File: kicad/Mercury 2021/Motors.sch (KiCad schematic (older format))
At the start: 13 parts, among them J15 Raspberry_Pi_2_3, J22 Servos_Connector, J23 Pi_Extra_Comm, J24 Pi_Extra_GPIO, J25 Pi_Extra_GPIO, J26 Pi_Extra_Power, J27 Pi_Extra_GND, J28 Pi_Extra_GPIO, J29 Pi_Extra_GPIO, J38 USB_B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

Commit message: Updated new board
- Did PCB traces
-- almost got away with just 2 copper layers, pi ruined it when there was only a bit to go. Probably possible but would take a lot of back and forth
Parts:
- added U12D1, U12E1: PCA9685, Connector_PinSocket_2.54mm:PinSocket_1x03_P2.54mm_Vertical, symbol Mercury:PCA9685
- J22: footprint Connector_PinSocket_2.54mm:PinSocket_2x03_P2.54mm_Vertical -> Connector_PinHeader_2.54mm:PinHeader_2x03_P2.54mm_Vertical; symbol Connector_Generic:Conn_02x03_Counter_Clockwise -> Connector_Generic:Conn_02x03_Top_Bottom
- U11, U13: footprint Connector_PinHeader_2.54mm:PinHeader_1x05_P2.54mm_Vertical -> Connector_JST:JST_EH_B5B-EH-A_1x05_P2.50mm_Vertical
- U12: footprint Connector_PinHeader_2.54mm:PinHeader_1x06_P2.54mm_Vertical -> Connector_PinSocket_2.54mm:PinSocket_1x06_P2.54mm_Vertical
- U12A1, U12B1: renamed from U12; footprint Connector_PinHeader_2.54mm:PinHeader_1x06_P2.54mm_Vertical -> Connector_PinSocket_2.54mm:PinSocket_1x03_P2.54mm_Vertical
- U12C1: renamed from U12; footprint Connector_PinHeader_2.54mm:PinHeader_1x06_P2.54mm_Vertical -> TerminalBlock:TerminalBlock_Altech_AK300-2_P5.00mm
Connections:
- net Serco_VCC is gone; now on net Servo_VCC: U12.5 (VCC)
- net Pi_5v: no longer J15.4 (5V), J26.1 (Pin_1), J26.2 (Pin_2)
- net Pi_GND: now also J15.39 (GND); no longer J15.20 (GND), J15.25 (GND), J15.30 (GND), J15.34 (GND), J27.1 (Pin_1), J27.2 (Pin_2), J27.3 (Pin_3), J27.4 (Pin_4), J27.5 (Pin_5)
- net at U12B1.1 (PWM_1): now also J22.4 (Pin_4); no longer J22.6 (Pin_6)
- net at U12B1.3 (GND): now also J22.6 (Pin_6); no longer J22.4 (Pin_4)
- net Pi_3v3 renamed Pi_3v3a
- net Pi_3v3a: no longer J15.17 (3V3), J26.5 (Pin_5)
- net SUB_D- renamed USB_D-
- new net Pi_3v3b: J15.17 (3V3), J26.5 (Pin_5)
- new net Pi_5v_a: J15.4 (5V), J26.2 (Pin_2)
- new net Pi_GNDa: J15.20 (GND), J27.5 (Pin_5)
- new net Pi_GNDb: J15.25 (GND), J27.4 (Pin_4)
- new net Pi_GNDc: J15.30 (GND), J27.3 (Pin_3)
- new net Pi_GNDe: J15.34 (GND), J27.2 (Pin_2)
- no-connect marks 4 -> 10
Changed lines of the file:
@@
 F 0 "U11" H 812 1075 50  0000 C CNN
 F 1 "PCA9685" H 812 984 50  0000 C CNN
-F 2 "Connector_PinHeader_2.54mm:PinHeader_1x05_P2.54mm_Vertical" H 750 1000 50  0001 C CNN
+F 2 "Connector_JST:JST_EH_B5B-EH-A_1x05_P2.50mm_Vertical" H 750 1000 50  0001 C CNN
 F 3 "" H 750 1000 50  0001 C CNN
 	3    750  800
@@
 F 0 "U13" H 812 2025 50  0000 C CNN
 F 1 "PCA9685" H 812 1934 50  0000 C CNN
-F 2 "Connector_PinHeader_2.54mm:PinHeader_1x05_P2.54mm_Vertical" H 750 1950 50  0001 C CNN
+F 2 "Connector_JST:JST_EH_B5B-EH-A_1x05_P2.50mm_Vertical" H 750 1950 50  0001 C CNN
 F 3 "" H 750 1950 50  0001 C CNN
 	3    750  1750
@@
 F 0 "U11" H 3119 1451 50  0000 L CNN
 F 1 "PCA9685" H 3119 1360 50  0000 L CNN
-F 2 "Connector_PinHeader_2.54mm:PinHeader_1x05_P2.54mm_Vertical" H 2800 1750 50  0001 C CNN
+F 2 "Connector_JST:JST_EH_B5B-EH-A_1x05_P2.50mm_Vertical" H 2800 1750 50  0001 C CNN
 F 3 "" H 2800 1750 50  0001 C CNN
 	1    2800 1550
@@
 F 0 "U13" H 3119 2051 50  0000 L CNN
 F 1 "PCA9685" H 3119 1960 50  0000 L CNN
-F 2 "Connector_PinHeader_2.54mm:PinHeader_1x05_P2.54mm_Vertical" H 2800 2350 50  0001 C CNN
+F 2 "Connector_JST:JST_EH_B5B-EH-A_1x05_P2.50mm_Vertical" H 2800 2350 50  0001 C CNN
 F 3 "" H 2800 2350 50  0001 C CNN
 	1    2800 2150
@@
 	5650 2200 5450 2200
 Entry Wire Line
-	5300 1700 5400 1800
+	5350 1700 5450 1800
 Entry Wire Line
 	5350 1900 5450 2000
@@
 Wire Bus Line
 	5350 2800 5350 3700
-$Comp
-L Mercury:PCA9685 U12
-U 2 1 609948C9
-P 3800 1300
-F 0 "U12" H 3969 950 50  0000 L CNN
-F 1 "PCA9685" H 3969 859 50  0000 L CNN
-F 2 "Connector_PinHeader_2.54mm:PinHeader_1x06_P2.54mm_Vertical" H 3800 1500 50  0001 C CNN
-F 3 "" H 3800 1500 50  0001 C CNN
-	2    3800 1300
-	-1   0    0    1
-$EndComp
 Entry Wire Line
 	3450 650  3350 750
@@
 AR Path="/6098200C" Ref="U?"  Part="3"
 AR Path="/609567C6/6098200C" Ref="U?"  Part="3"
-AR Path="/60979A3C/6098200C" Ref="U12"  Part="3"
-F 0 "U12" V 1000 1150 50  0000 L CNN
+AR Path="/60979A3C/6098200C" Ref="U12C1"  Part="3"
+F 0 "U12C1" V 1000 1150 50  0000 L CNN
 F 1 "PCA9685" V 900 1100 50  0000 L CNN
-F 2 "Connector_PinHeader_2.54mm:PinHeader_1x06_P2.54mm_Vertical" H 750 1450 50  0001 C CNN
+F 2 "TerminalBlock:TerminalBlock_Altech_AK300-2_P5.00mm" H 750 1450 50  0001 C CNN
 F 3 "" H 750 1450 50  0001 C CNN
 	3    750  1250
@@
 MotorPower
 $Comp
-L Connector_Generic:Conn_02x03_Counter_Clockwise J22
+L Connector_Generic:Conn_02x03_Top_Bottom J22
 U 1 1 609CB3BE
 P 4650 800
 F 0 "J22" H 4700 1117 50  0000 C CNN
 F 1 "Servos_Connector" H 4700 1026 50  0000 C CNN
-F 2 "Connector_PinSocket_2.54mm:PinSocket_2x03_P2.54mm_Vertical" H 4650 800 50  0001 C CNN
+F 2 "Connector_PinHeader_2.54mm:PinHeader_2x03_P2.54mm_Vertical" H 4650 800 50  0001 C CNN
 F 3 "~" H 4650 800 50  0001 C CNN
 	1    4650 800
 	1    0    0    -1
-$EndComp
-$Comp
-L Mercury:PCA9685 U12
-U 4 1 609BDBFC
-P 4550 800
-F 0 "U12" H 4708 484 50  0000 L CNN
-F 1 "PCA9685" H 4708 393 50  0000 L CNN
-F 2 "Connector_PinHeader_2.54mm:PinHeader_1x06_P2.54mm_Vertical" H 4550 1000 50  0001 C CNN
-F 3 "" H 4550 1000 50  0001 C CNN
-	4    4550 800
-	0    1    1    0
 $EndComp
 $Comp
@@
 	1    0    0    -1
 $EndComp
-Wire Wire Line
-	7250 1500 7300 1500
-Wire Wire Line
-	7250 1500 7250 1900
 Wire Wire Line
 	7250 1300 7300 1300
@@
 	6350 3500 6350 3550
 Text Label 6350 3550 1    50   ~ 0
-Pi_GND
+Pi_GNDa
 Text Label 6450 3550 1    50   ~ 0
-Pi_GND
+Pi_GNDb
 Text Label 6550 3550 1    50   ~ 0
-Pi_GND
+Pi_GNDc
 Text Label 6650 3550 1    50   ~ 0
-Pi_GND
-Text Label 6750 3550 1    50   ~ 0
-Pi_GND
+Pi_GNDe
+Text Label 7100 3600 2    50   ~ 0
+Pi_GNDf
 NoConn ~ 6450 850
 Text Label 6650 850  1    50   ~ 0
-Pi_3v3
+Pi_3v3b
 Text Label 6550 850  1    50   ~ 0
-Pi_3v3
+Pi_3v3a
 Text Label 6350 850  1    50   ~ 0
-Pi_5v
-Text Label 6250 850  1    50   ~ 0
-Pi_5v
+Pi_5v_a
 Wire Wire Line
 	6650 850  6650 900
@@
 Wire Wire Line
 	4400 700  4450 700
-$Comp
-L Mercury:PCA9685 U12
-U 5 1 609BF816
-P 5100 850
-F 0 "U12" H 5258 534 50  0000 L CNN
-F 1 "PCA9685" H 5258 443 50  0000 L CNN
-F 2 "Connector_PinHeader_2.54mm:PinHeader_1x06_P2.54mm_Vertical" H 5100 1050 50  0001 C CNN
-F 3 "" H 5100 1050 50  0001 C CNN
-	5    5100 850
-	0    1    1    0
-$EndComp
 Wire Wire Line
 	5000 700  5000 750
@@
 Wire Wire Line
 	5250 2450 5250 2500
-Text Label 5200 2450 2    50   ~ 0
-Pi_5v
 Wire Wire Line
 	6750 3500 7100 3500
@@
 	1550 2450 1450 2350
 Text Label 1400 2350 2    50   ~ 0
-Pi_5v
+Pi_5vin
 Entry Wire Line
 	1300 2350 1200 2450
@@
 Entry Wire Line
 	9250 1600 9350 1700
-Wire Bus Line
-	2450 2250 2450 2400
-Wire Bus Line
-	2450 1650 2450 1800
-Wire Bus Line
-	1550 2800 5350 2800
-Wire Bus Line
-	2450 1400 2450 1650
-Wire Bus Line
-	2450 2000 2450 2250
-Wire Bus Line
-	5350 3700 7550 3700
-Wire Bus Line
-	5350 1700 5350 2800
-Wire Bus Line
-	1550 1750 1550 2800
-Wire Bus Line
-	9350 1450 9350 1750
-Wire Bus Line
-	3350 750  3350 1400
-Wire Bus Line
-	7550 1550 7550 3700
-Wire Bus Line
-	1200 850  1200 2450
 Text HLabel 9350 1750 2    50   Input ~ 0
 USB_BUS
@@
 USB_D+
 Text GLabel 9050 1550 2    50   Input ~ 0
-SUB_D-
+USB_D-
 Text GLabel 9150 1750 2    50   Input ~ 0
 USB_SHIELD
@@
 	1    0    0    -1
 $EndComp
+$Comp
+L Mercury:PCA9685 U12B1
+U 5 1 609BF816
+P 5100 850
+F 0 "U12B1" H 5000 850 50  0000 L CNN
+F 1 "PCA9685" H 4700 950 50  0000 L CNN
+F 2 "Connector_PinSocket_2.54mm:PinSocket_1x03_P2.54mm_Vertical" H 5100 1050 50  0001 C CNN
+F 3 "" H 5100 1050 50  0001 C CNN
+	5    5100 850
+	0    1    1    0
+$EndComp
+$Comp
+L Mercury:PCA9685 U12A1
+U 4 1 609BDBFC
+P 4550 800
+F 0 "U12A1" H 4708 484 50  0000 L CNN
+F 1 "PCA9685" H 4708 393 50  0000 L CNN
+F 2 "Connector_PinSocket_2.54mm:PinSocket_1x03_P2.54mm_Vertical" H 4550 1000 50  0001 C CNN
+F 3 "" H 4550 1000 50  0001 C CNN
+	4    4550 800
+	0    1    1    0
+$EndComp
+$Comp
+L Mercury:PCA9685 U12
+U 2 1 609948C9
+P 3800 1300
+F 0 "U12" H 3969 950 50  0000 L CNN
+F 1 "PCA9685" H 3969 859 50  0000 L CNN
+F 2 "Connector_PinSocket_2.54mm:PinSocket_1x06_P2.54mm_Vertical" H 3800 1500 50  0001 C CNN
+F 3 "" H 3800 1500 50  0001 C CNN
+	2    3800 1300
+	-1   0    0    1
+$EndComp
+$Comp
+L Mercury:PCA9685 U12D1
+U 6 1 6141A1DE
+P 4100 1600
+F 0 "U12D1" V 4131 981 50  0000 R CNN
+F 1 "PCA9685" V 4040 981 50  0000 R CNN
+F 2 "Connector_PinSocket_2.54mm:PinSocket_1x03_P2.54mm_Vertical" H 4100 1800 50  0001 C CNN
+F 3 "" H 4100 1800 50  0001 C CNN
+	6    4100 1600
+	0    -1   -1   0
+$EndComp
+$Comp
+L Mercury:PCA9685 U12E1
+U 7 1 6141EE79
+P 4300 1600
+F 0 "U12E1" V 3975 1237 50  0000 C CNN
+F 1 "PCA9685" V 4066 1237 50  0000 C CNN
+F 2 "Connector_PinSocket_2.54mm:PinSocket_1x03_P2.54mm_Vertical" V 4067 1237 50  0001 C CNN
+F 3 "" H 4300 1800 50  0001 C CNN
+	7    4300 1600
+	0    1    1    0
+$EndComp
+NoConn ~ 4150 1500
+NoConn ~ 4250 1500
+NoConn ~ 4250 1600
+NoConn ~ 4150 1600
+NoConn ~ 4150 1700
+NoConn ~ 4250 1700
+Text GLabel 3500 750  2    50   Input ~ 0
+Servo_VCC
+Wire Wire Line
+	7300 1500 7300 1900
+Wire Wire Line
+	7300 1900 7250 1900
+Text Label 6250 900  2    50   ~ 0
+Pi_5vin
+Text Label 1450 2600 3    50   ~ 0
+Pi_GNDf
+Wire Wire Line
+	1350 2600 1450 2600
+Entry Wire Line
+	1450 2600 1550 2500
+Wire Bus Line
+	1550 2800 5350 2800
+Wire Bus Line
+	2450 2250 2450 2400
+Wire Bus Line
+	2450 1650 2450 1800
+Wire Bus Line
+	2450 1400 2450 1650
+Wire Bus Line
+	2450 2000 2450 2250
+Wire Bus Line
+	5350 3700 7550 3700
+Wire Bus Line
+	5350 1700 5350 2800
+Wire Bus Line
+	1550 1750 1550 2800
+Wire Bus Line
+	3350 750  3350 1400
+Wire Bus Line
+	7550 1550 7550 3700
+Wire Bus Line
+	9350 1450 9350 1750
+Wire Bus Line
+	1200 850  1200 2450
+Text GLabel 1350 2600 2    50   Input ~ 0
+Pi_GND
 $EndSCHEMATC

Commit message: New New board
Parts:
- removed J22: Servos_Connector, Connector_PinHeader_2.54mm:PinHeader_2x03_P2.54mm_Vertical, symbol Connector_Generic:Conn_02x03_Top_Bottom
- removed J23: Pi_Extra_Comm, Connector_PinSocket_2.54mm:PinSocket_1x02_P2.54mm_Vertical, symbol Connector:Conn_01x02_Female
- removed J24: Pi_Extra_GPIO, Connector_PinSocket_2.54mm:PinSocket_1x02_P2.54mm_Vertical, symbol Connector:Conn_01x02_Female
- removed J25: Pi_Extra_GPIO, Connector_PinSocket_2.54mm:PinSocket_1x06_P2.54mm_Vertical, symbol Connector:Conn_01x06_Female
- removed J26: Pi_Extra_Power, Connector_PinSocket_2.54mm:PinSocket_1x05_P2.54mm_Vertical, symbol Connector:Conn_01x05_Female
- removed J27: Pi_Extra_GND, Connector_PinSocket_2.54mm:PinSocket_1x05_P2.54mm_Vertical, symbol Connector:Conn_01x05_Female
- removed J28: Pi_Extra_GPIO, Connector_PinSocket_2.54mm:PinSocket_1x03_P2.54mm_Vertical, symbol Connector:Conn_01x03_Female
- removed J29: Pi_Extra_GPIO, Connector_PinSocket_2.54mm:PinSocket_1x05_P2.54mm_Vertical, symbol Connector:Conn_01x05_Female
- removed J38: USB_B, Connector_USB:USB_B_TE_5787834_Vertical, symbol Connector:USB_B
- removed U12A1, U12B1, U12D1, U12E1: PCA9685, Connector_PinSocket_2.54mm:PinSocket_1x03_P2.54mm_Vertical, symbol Mercury:PCA9685
- added J2, J3: Conn_01x20_Female, Connector_PinSocket_2.54mm:PinSocket_1x20_P2.54mm_Vertical, symbol Connector:Conn_01x20_Female
- U11, U13: value PCA9685 -> MDD10A
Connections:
- net LM_DIR1_GPIO6: now also J2.16 (Pin_16)
- net LM_DIR2_GPIO5: now also J2.15 (Pin_15)
- net LM_GND: now also J3.3 (Pin_3)
- net LM_PWM1_GPIO19: now also J2.18 (Pin_18)
- net LM_PWM2_GPIO13: now also J2.17 (Pin_17)
- net Pi_5v: now also J3.1 (Pin_1)
- net Pi_GND: now also J2.20 (Pin_20)
- net Pi_3v3a renamed Pi01
- net Pi01: now also J2.1 (Pin_1)
- net Pi_3v3b renamed Pi17
- net Pi17: now also J2.9 (Pin_9)
- net Pi_5v_a renamed Pi04
- net Pi04: now also J3.2 (Pin_2)
- net Pi_GNDa renamed Pi20
- net Pi20: now also J3.10 (Pin_10)
- net Pi_GNDb renamed Pi25
- net Pi25: now also J2.13 (Pin_13)
- net Pi_GNDc renamed Pi30
- net Pi30: now also J3.15 (Pin_15)
- net Pi_GNDe renamed Pi34
- net Pi34: now also J3.17 (Pin_17)
- net Pi_GPIO00 renamed Pi27
- net Pi27: now also J2.14 (Pin_14)
- net Pi_GPIO01 renamed Pi28
- net Pi28: now also J3.14 (Pin_14)
- net Pi_GPIO04 renamed Pi07
- net Pi07: now also J2.4 (Pin_4)
- net Pi_GPIO07 renamed Pi26
- net Pi26: now also J3.13 (Pin_13)
- net Pi_GPIO08 renamed Pi24
- net Pi24: now also J3.12 (Pin_12)
- net Pi_GPIO09 renamed Pi21
- net Pi21: now also J2.11 (Pin_11)
- net Pi_GPIO10 renamed Pi19
- net Pi19: now also J2.10 (Pin_10)
- net Pi_GPIO11 renamed Pi23
- net Pi23: now also J2.12 (Pin_12)
- net Pi_GPIO14 renamed Pi08
- net Pi08: now also J3.4 (Pin_4)
- net Pi_GPIO15 renamed Pi10
- net Pi10: now also J3.5 (Pin_5)
- net Pi_GPIO16 renamed Pi36
- net Pi36: now also J3.18 (Pin_18)
- net Pi_GPIO17 renamed Pi11
- net Pi11: now also J2.6 (Pin_6)
- net Pi_GPIO22 renamed Pi15
- net Pi15: now also J2.8 (Pin_8)
- net Pi_GPIO23 renamed Pi16
- net Pi16: now also J3.8 (Pin_8)
- net Pi_GPIO24 renamed Pi18
- net Pi18: now also J3.9 (Pin_9)
- net Pi_GPIO25 renamed Pi22
- net Pi22: now also J3.11 (Pin_11)
- net Pi_GPIO26 renamed Pi37
- net Pi37: now also J2.19 (Pin_19)
- net Pi_GPIO27 renamed Pi13
- net Pi13: now also J2.7 (Pin_7)
- net RM_DIR1_GPIO20 renamed Pi38
- net Pi38: now also J3.19 (Pin_19)
- net RM_DIR2_GPIO21 renamed Pi40
- net Pi40: now also J3.20 (Pin_20)
- net RM_GND renamed Pi09
- net Pi09: now also J2.5 (Pin_5)
- net RM_PWM1_GPIO18 renamed Pi12
- net Pi12: now also J3.6 (Pin_6)
- net RM_PWM2_GPIO12 renamed Pi32
- net Pi32: now also J3.16 (Pin_16)
- net Servo_CTL_GND renamed Pi14
- net Pi14: now also J3.7 (Pin_7)
- net Servo_SCL renamed Pi05
- net Pi05: now also J2.3 (Pin_3)
- net Servo_SDA renamed Pi03
- net Pi03: now also J2.2 (Pin_2)
- no-connect marks 10 -> 2

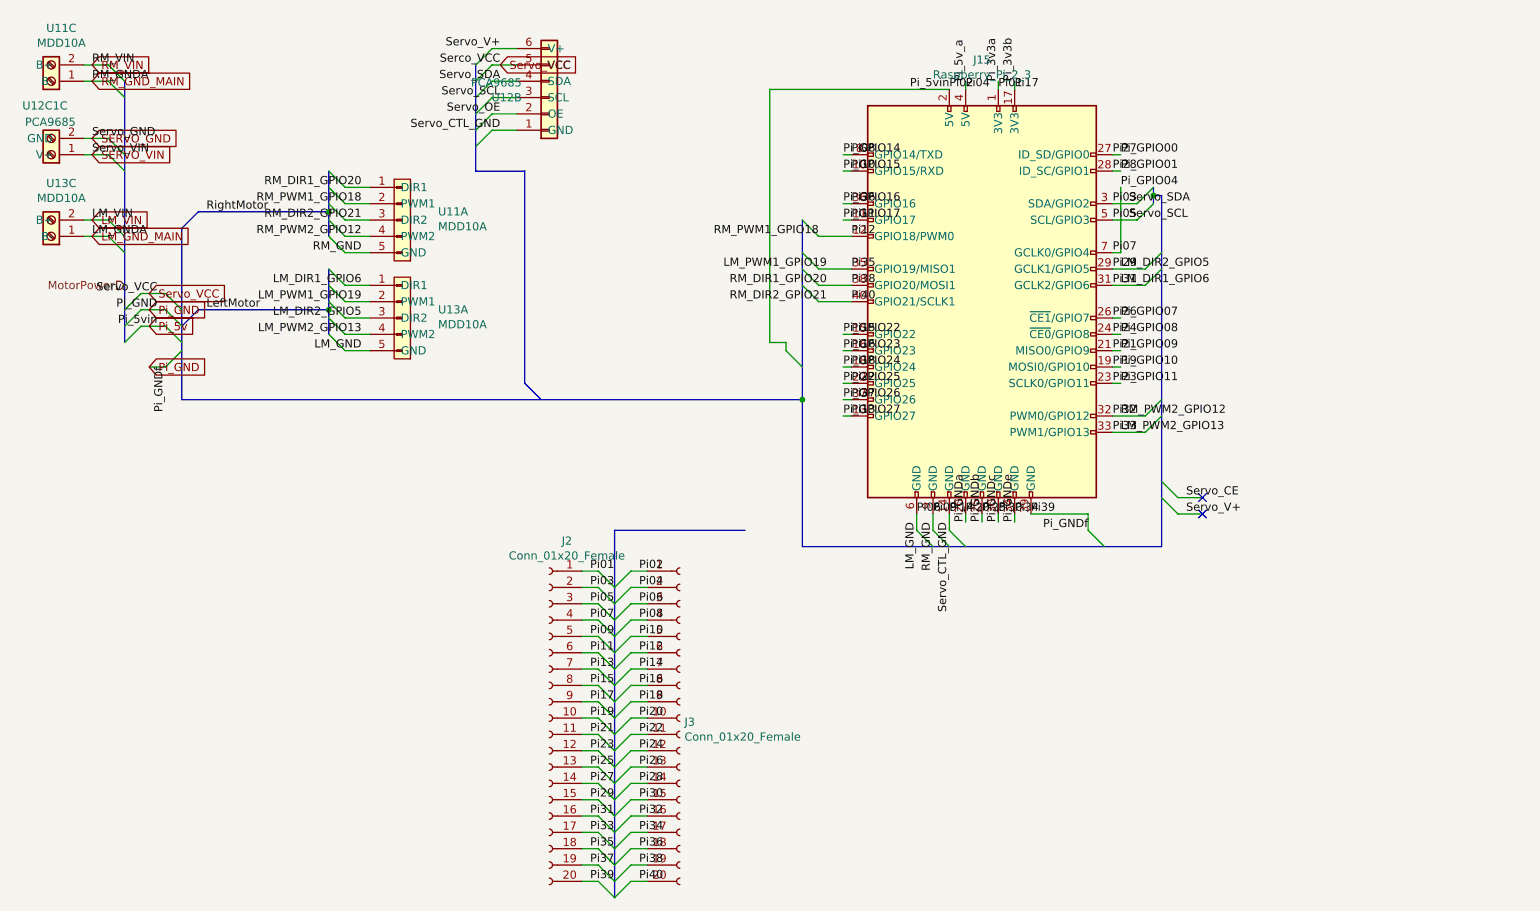
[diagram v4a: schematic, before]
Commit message: NOTE! Updated PCB
This is different than the PCBs that were ordered.
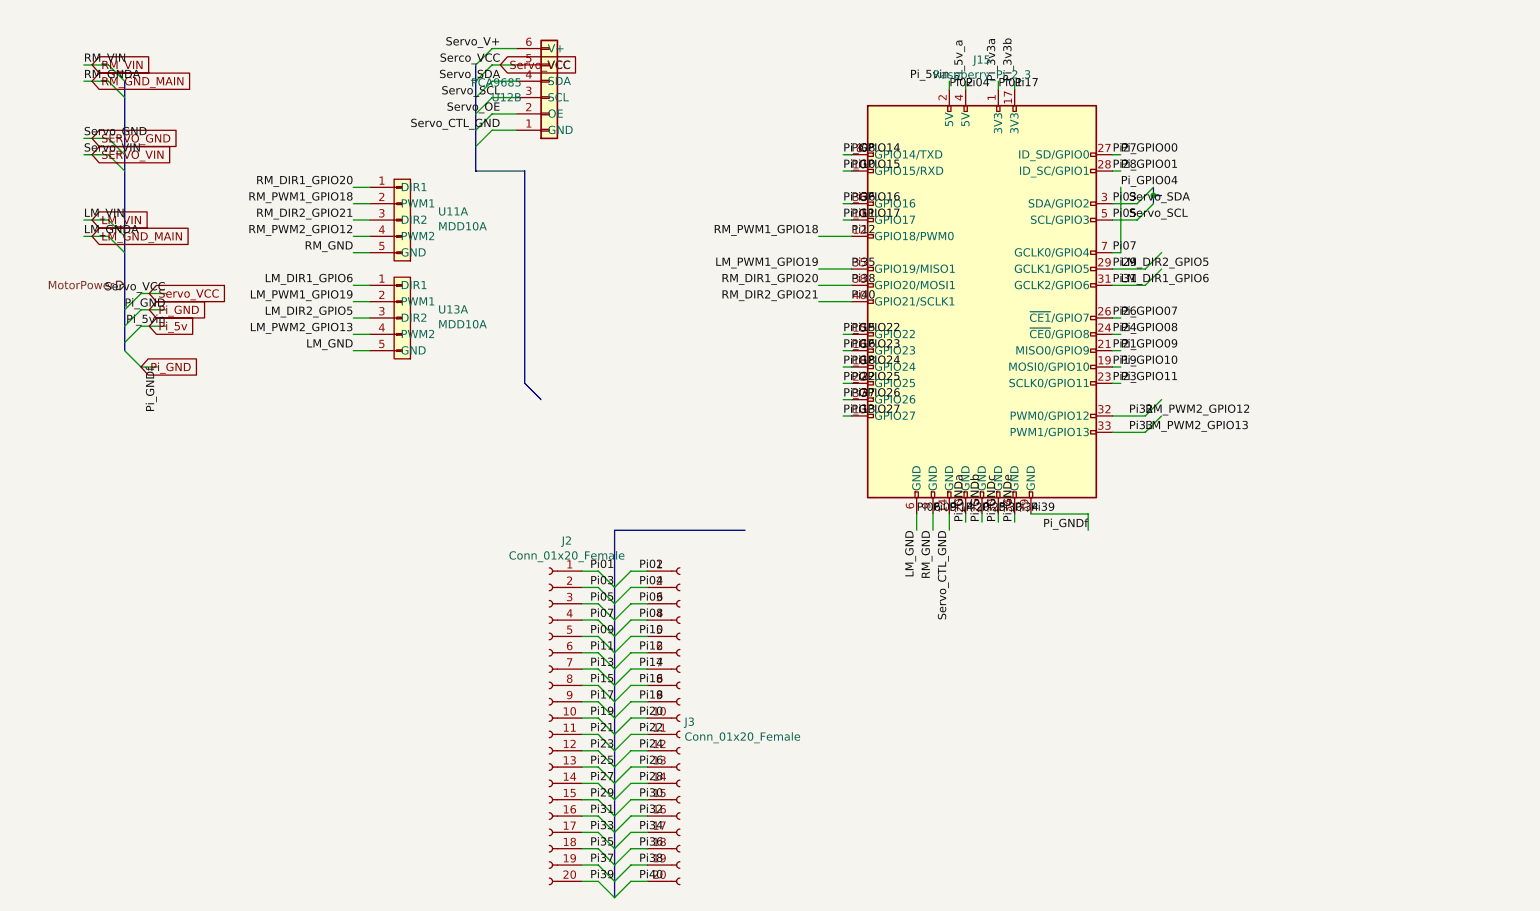
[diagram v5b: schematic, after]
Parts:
- removed unit 3 of U11
- removed U12C1: PCA9685, TerminalBlock:TerminalBlock_Altech_AK300-2_P5.00mm, symbol Mercury:PCA9685
- removed unit 3 of U13
- J15: footprint Connector_PinSocket_2.54mm:PinSocket_2x20_P2.54mm_Horizontal -> Connector_PinSocket_2.54mm:PinSocket_2x20_P2.54mm_Vertical
- U11, U13: footprint Connector_JST:JST_EH_B5B-EH-A_1x05_P2.50mm_Vertical -> Connector_PinSocket_2.54mm:PinSocket_1x05_P2.54mm_Vertical
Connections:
- no-connect marks 2 -> 0

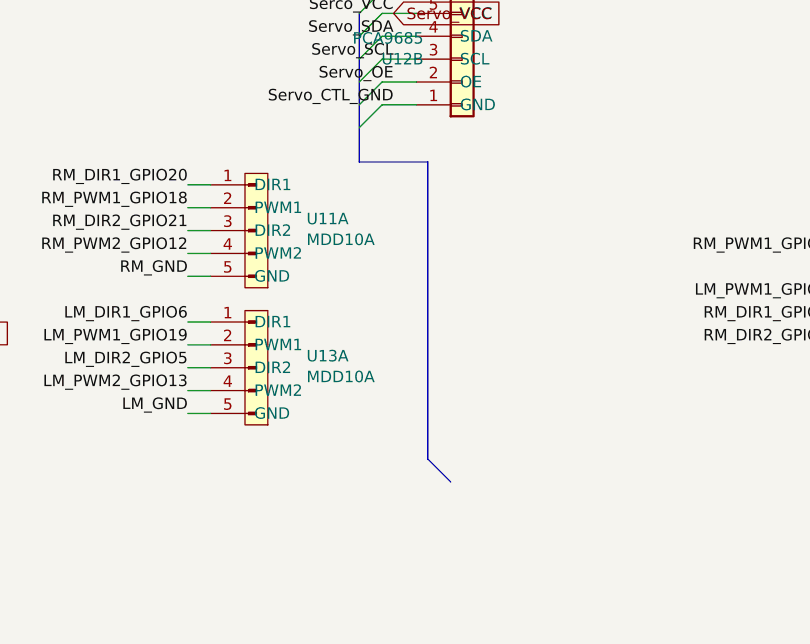
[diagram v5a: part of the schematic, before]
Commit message: Updated PCB
Updated Labels & arduino now powered off of board.
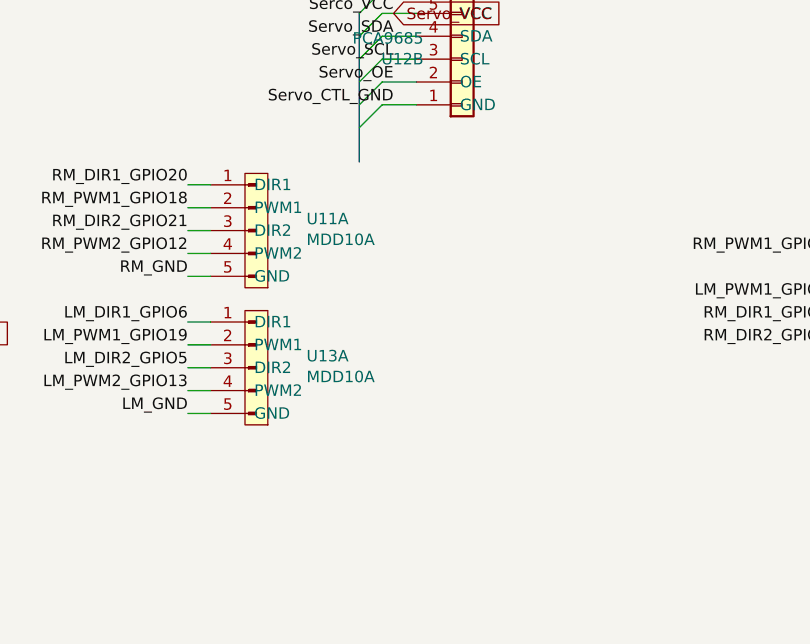
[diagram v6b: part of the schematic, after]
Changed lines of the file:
@@
 Entry Wire Line
 	3450 1150 3350 1250
-Wire Bus Line
-	3350 1400 3650 1400
-Entry Bus Bus
-	3650 2700 3750 2800
-Wire Bus Line
-	3650 1400 3650 2700
 Wire Wire Line
 	3600 650  3450 650
